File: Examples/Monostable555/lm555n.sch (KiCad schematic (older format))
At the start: 17 parts, among them Q1 QNOM, U1 PORT, U2 ADC8, U3 DAC8, U4 LIMIT8, U5 D_INVERTER, U6 D_SRLATCH

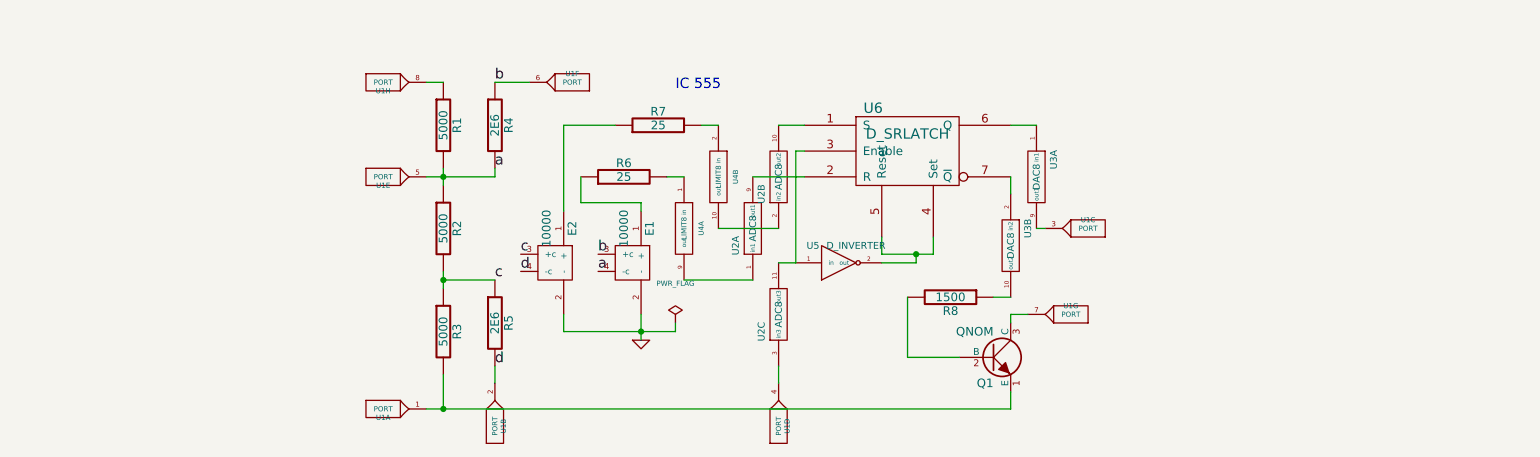
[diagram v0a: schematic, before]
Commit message: lm555 subcircuit modified
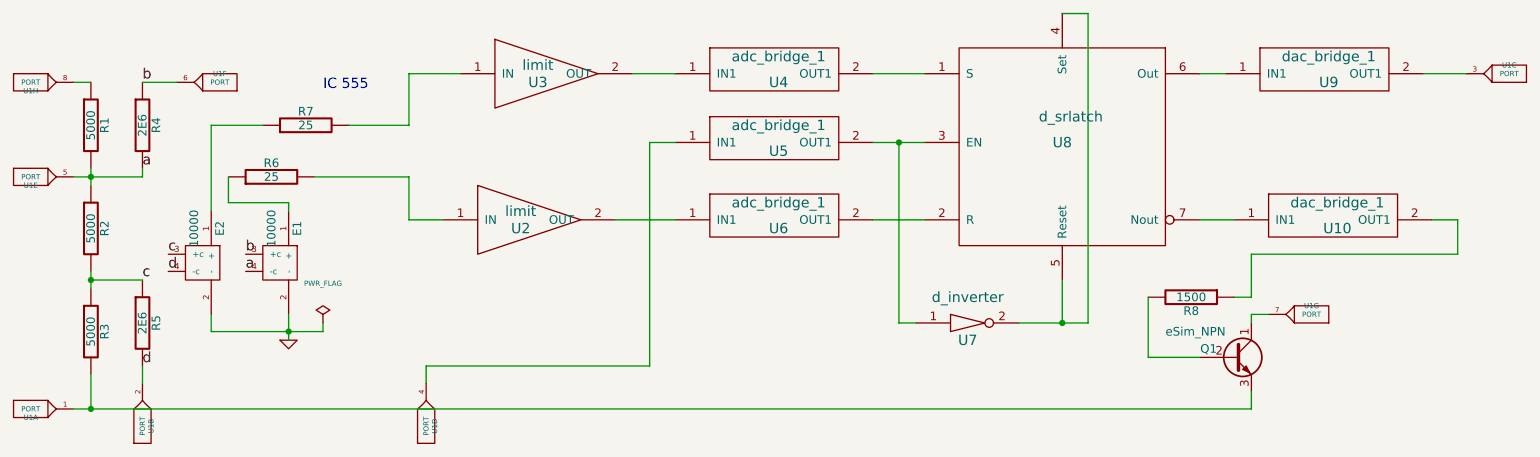
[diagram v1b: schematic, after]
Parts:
- removed Q1: QNOM, symbol NPN
- removed U2: ADC8, symbol ADC8
- removed U3: DAC8, symbol DAC8
- removed U4: LIMIT8, symbol LIMIT8
- removed U5: D_INVERTER, symbol d_inverter-RESCUE-lm555n
- removed U6: D_SRLATCH, symbol D_SRLatch
- added Q1: eSim_NPN, symbol eSim_NPN
- added U10, U9: dac_bridge_1, symbol dac_bridge_1
- added U2, U3: limit, symbol limit
- added U4, U5, U6: adc_bridge_1, symbol adc_bridge_1
- added U7: d_inverter, symbol d_inverter
- added U8: d_srlatch, symbol d_srlatch
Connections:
- net at R3.2, U1.1: now also Q1.3 (E)
- net at R6.2: now also U2.1 (IN)
- net at R7.2: now also U3.1 (IN)
- net at R8.2: now also Q1.2 (B)
- net at U1.7: now also Q1.1 (C)
- net at R8.1: now also U10.2 (OUT1)
- net at U1.3: now also U9.2 (OUT1)
- net at U1.4: now also U5.1 (IN1)
- new net: U4.2 (OUT1), U8.1 (S)
- new net: U6.2 (OUT1), U8.2 (R)
- new net: U5.2 (OUT1), U7.1, U8.3 (EN)
- new net: U7.2, U8.4 (Set), U8.5 (Reset)
- new net: U8.6 (Out), U9.1 (IN1)
- new net: U10.1 (IN1), U8.7 (Nout)
- new net: U3.2 (OUT), U4.1 (IN1)
- new net: U2.2 (OUT), U6.1 (IN1)
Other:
- moved on the sheet: E1, E2, R1, R2, R3, R4, R5, R6, R7, R8, U1A, U1B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
